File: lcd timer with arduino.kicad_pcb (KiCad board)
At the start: 2 copper layers, 121.1 x 76.4 mm, 33 parts, among them J1 Conn_01x05_Female, J2 Screw_Terminal_01x02, J3 Screw_Terminal_01x02, J4 Screw_Terminal_01x02, K1 SANYOU_SRD_Form_C, K2 SANYOU_SRD_Form_C, K3 SANYOU_SRD_Form_C, K4 SANYOU_SRD_Form_C, Q1 2N3904, Q2 2N3904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

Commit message: Version2
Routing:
- net on3: track 78.3 -> 75.6 mm

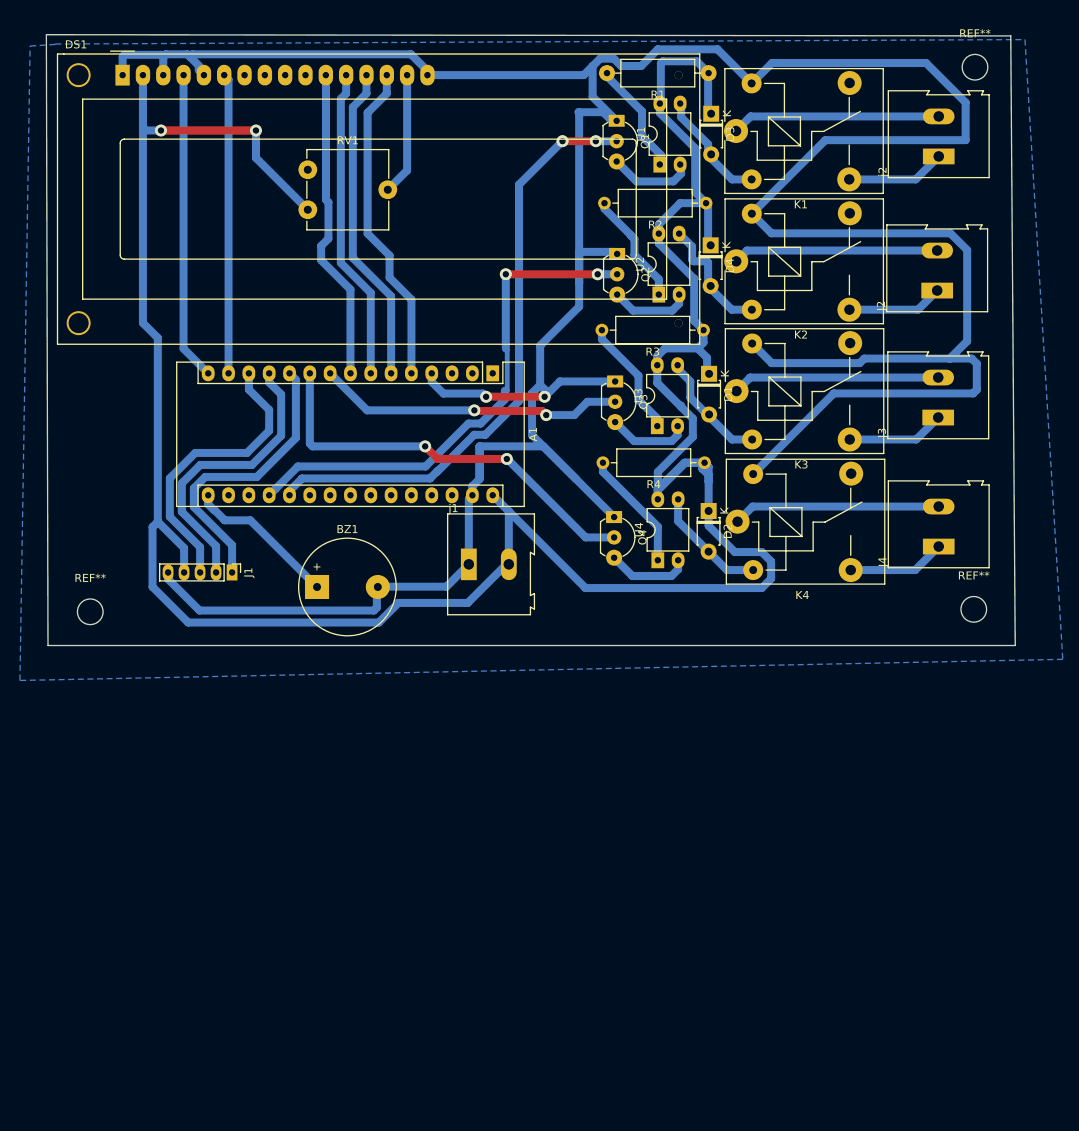
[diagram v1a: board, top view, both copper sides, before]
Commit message: thiker traces
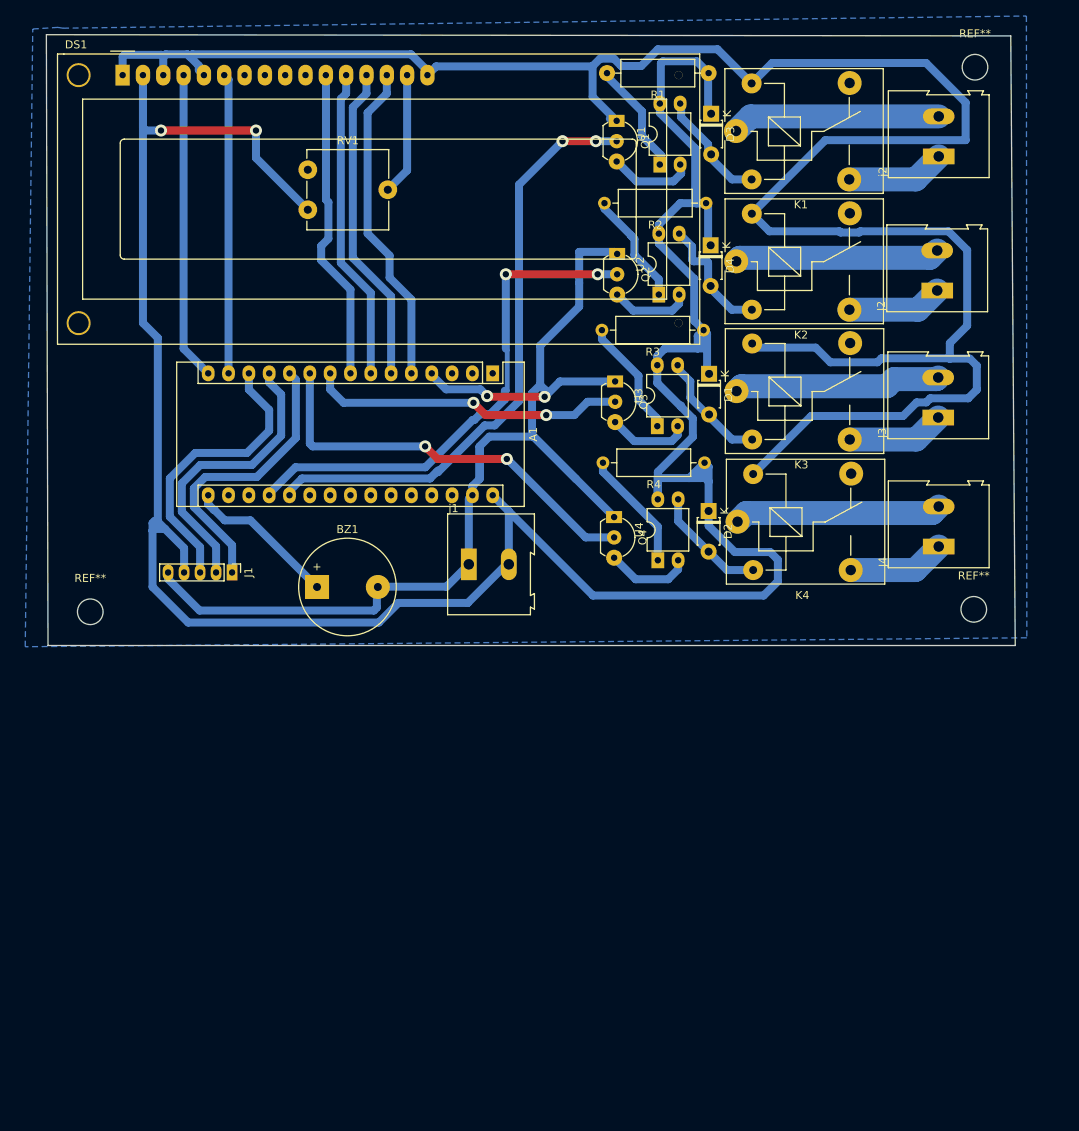
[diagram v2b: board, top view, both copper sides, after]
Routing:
- net -: track 448.1 -> 422.9 mm
- net +: track 335.0 -> 341.6 mm
- net on1: track 38.5 -> 39.6 mm

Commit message: removed acide traps
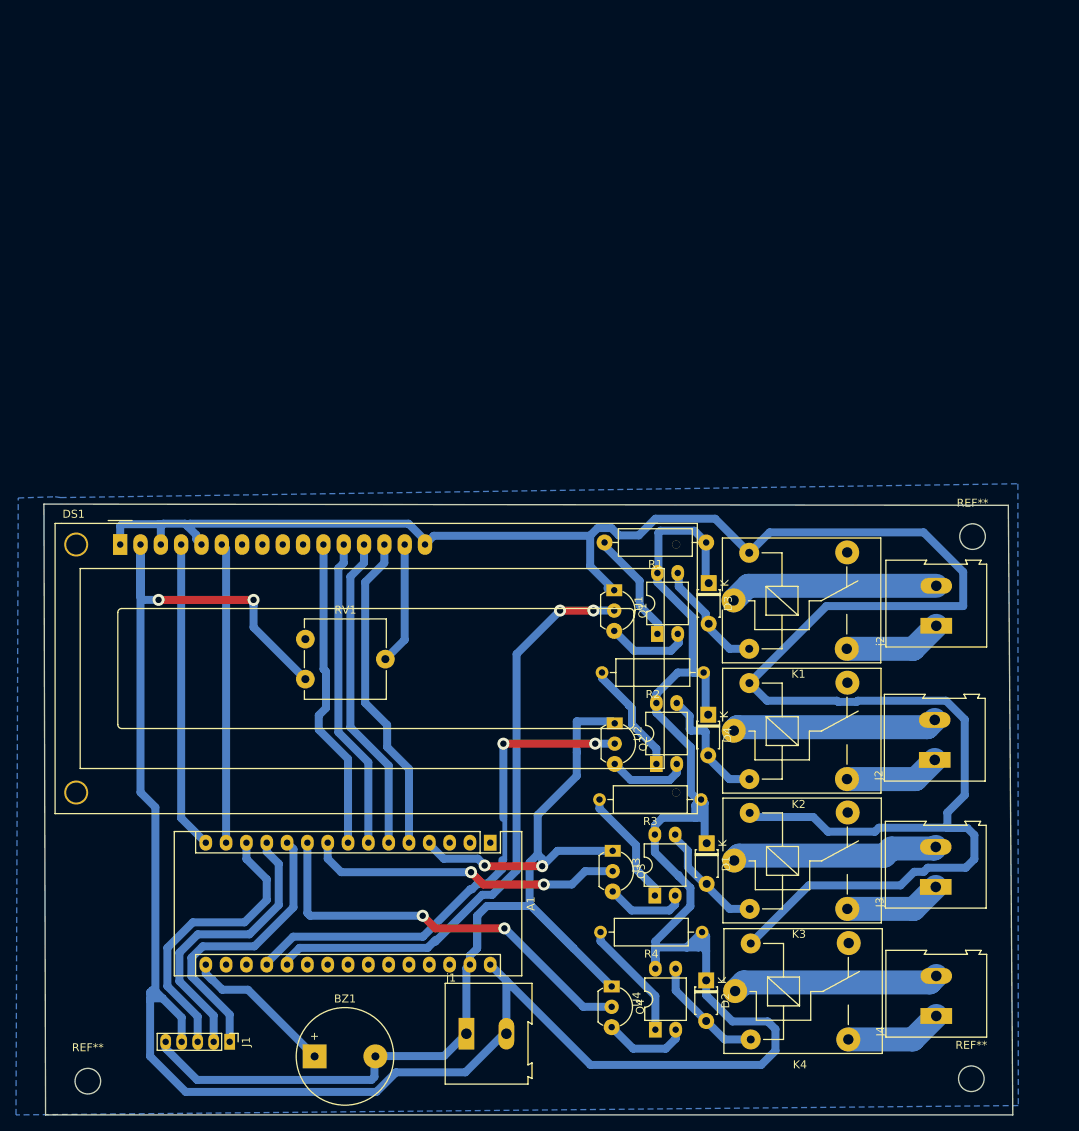
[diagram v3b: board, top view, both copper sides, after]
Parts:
- moved D1 58.7 mm to (150.0, 114.4)
- moved D2 58.7 mm to (149.9, 131.6)
- moved D3 58.7 mm to (150.3, 81.9)
- moved D4 58.7 mm to (150.2, 98.4)
- moved J1 58.7 mm to (90.4, 139.3)
- moved J2 58.7 mm to (178.5, 104.0)
- moved J3 58.7 mm to (178.6, 119.9)
- moved K2 58.7 mm to (153.4, 100.4)
- moved Q1 58.7 mm to (138.4, 82.8)
- moved Q4 58.7 mm to (138.1, 132.3)
- moved R4 58.7 mm to (149.4, 125.5)
- moved REF** 58.7 mm to (183.1, 143.9)
- moved REF** 58.7 mm to (72.6, 144.2)
- moved U4 58.7 mm to (143.6, 137.7)
- moved A1 58.7 mm to (122.9, 114.4)
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
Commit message: fixed the schematic
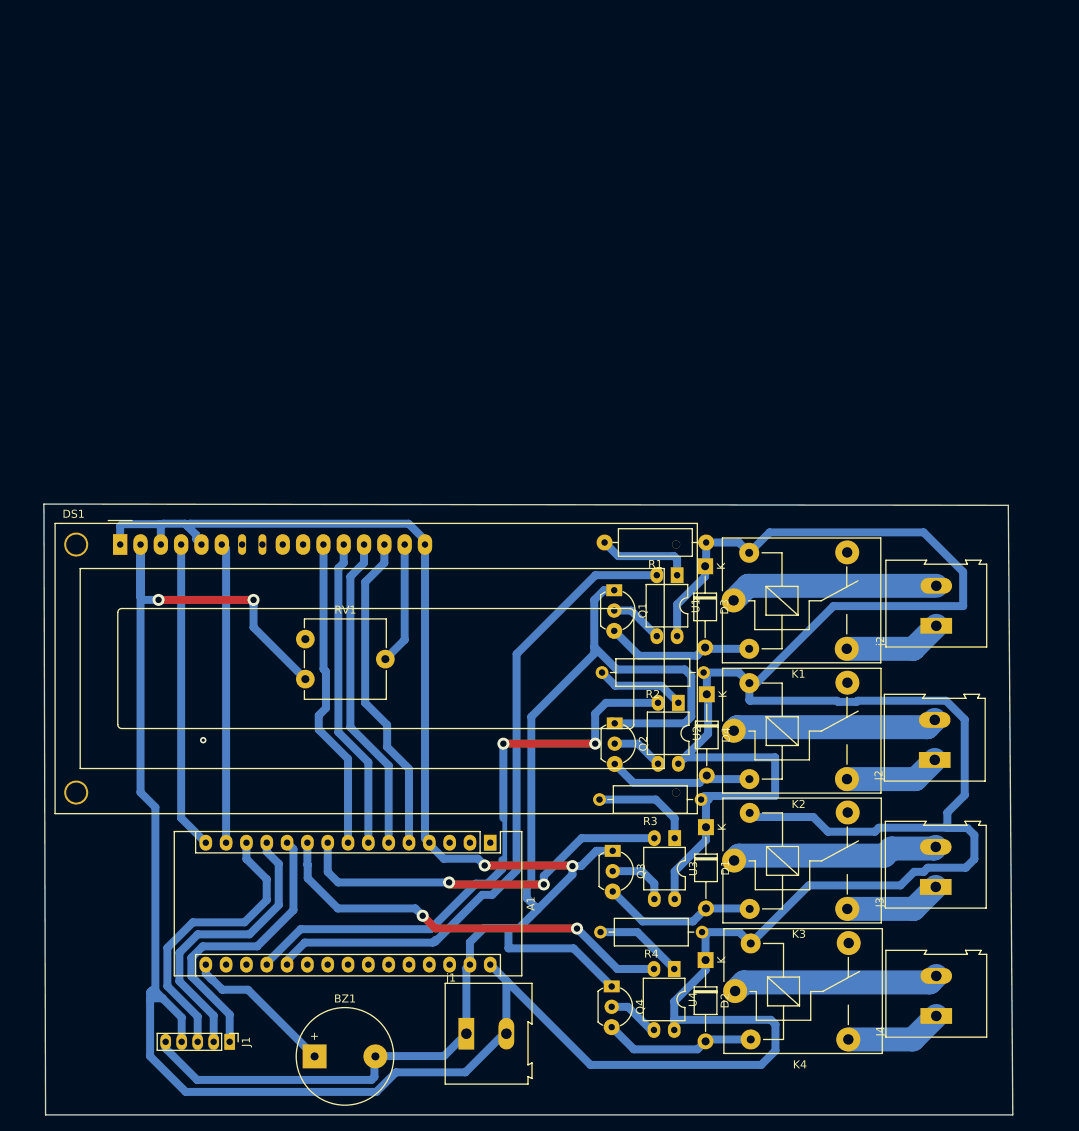
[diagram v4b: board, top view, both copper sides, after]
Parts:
- removed REF** (x3): MountingHole_3.2mm_M3, MountingHole:MountingHole_3.2mm_M3
- D1, D2, D3, D4: footprint Diode_THT:D_T-1_P5.08mm_Horizontal -> Diode_THT:D_T-1_P10.16mm_Horizontal
- moved U2 8.12 mm to (146.5, 96.9), turned to 270 degrees
- moved U4 7.94 mm to (145.9, 130.1), turned to 270 degrees
- moved U1 7.74 mm to (146.3, 80.9), turned to 270 degrees
- moved U3 7.59 mm to (146.0, 113.8), turned to 270 degrees
- moved D4 2.56 mm to (150.0, 95.8)
- moved D2 2.54 mm to (149.9, 129.0)
- moved D3 2.15 mm to (149.8, 79.8)
- moved D1 2.01 mm to (149.9, 112.4)
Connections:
- K1 pad 5: - -> +
- K2 pad 5: - -> +
- K3 pad 5: - -> +
- K4 pad 5: - -> +
- Q1 pad 2: on3 -> Net-(Q1-Pad2)
- Q1 pad 3: Net-(Q1-Pad3) -> Net-(D3-Pad2)
- Q2 pad 2: on4 -> Net-(Q2-Pad2)
- Q2 pad 3: Net-(Q2-Pad3) -> Net-(D4-Pad2)
- Q3 pad 2: on1 -> Net-(Q3-Pad2)
- Q3 pad 3: Net-(Q3-Pad3) -> Net-(D1-Pad2)
- Q4 pad 2: on2 -> Net-(Q4-Pad2)
- Q4 pad 3: Net-(Q4-Pad3) -> Net-(D2-Pad2)
- U1 pad 2: Net-(Q1-Pad3) -> on3
- U1 pad 3: Net-(D3-Pad2) -> Net-(Q1-Pad2)
- U2 pad 2: Net-(Q2-Pad3) -> on4
- U2 pad 3: Net-(D4-Pad2) -> Net-(Q2-Pad2)
- U3 pad 2: Net-(Q3-Pad3) -> on1
- U3 pad 3: Net-(D1-Pad2) -> Net-(Q3-Pad2)
- U4 pad 2: Net-(Q4-Pad3) -> on2
- U4 pad 3: Net-(D2-Pad2) -> Net-(Q4-Pad2)
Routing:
- net +: track 341.9 -> 497.8 mm
- net -: track 422.7 -> 274.9 mm
- net Net-(Q4-Pad3): track 10.8 -> 0.00 mm
- net Net-(Q1-Pad3): track 10.6 -> 0.00 mm
- net Net-(Q3-Pad3): track 10.2 -> 0.00 mm
- net Net-(Q2-Pad3): track 10.1 -> 0.00 mm
- net on4: track 64.5 -> 74.2 mm
- net on1: track 39.6 -> 48.2 mm
- net Net-(Q3-Pad2): track 0.00 -> 7.80 mm
- net on3: track 75.6 -> 82.8 mm, vias 2 -> 0
- net Net-(Q1-Pad2): track 0.00 -> 6.65 mm
- net Net-(Q4-Pad2): track 0.00 -> 6.48 mm
- net Net-(Q2-Pad2): track 0.00 -> 6.45 mm
- net Net-(D1-Pad2): track 14.6 -> 19.4 mm
- net Net-(D2-Pad2): track 14.6 -> 19.0 mm
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- removed copper zone on B.Cu, net -
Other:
- net class Default: clearance 0.4 -> 0.2
- rule trace_clearance: 0.4 -> 0.2

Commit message: fixed the schematic
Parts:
- added R5: 220, Resistor_THT:R_Axial_DIN0309_L9.0mm_D3.2mm_P12.70mm_Horizontal, F.Cu at (119.8, 88.6)
- moved RV1 11.2 mm to (109.7, 88.5), turned to 180 degrees
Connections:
- DS1 pad 15: Net-(DS1-Pad15) -> +
- DS1 pad 16: - -> Net-(DS1-Pad16)
- DS1 pad 3: - -> Net-(DS1-Pad3)
- RV1 pad 2: Net-(DS1-Pad15) -> Net-(DS1-Pad3)
- RV1 pad 3: Net-(RV1-Pad3) -> -
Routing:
- net Net-(DS1-Pad3): track 0.00 -> 27.7 mm, vias 0 -> 2
- net -: track 274.9 -> 301.5 mm
- net +: track 497.8 -> 518.5 mm
- net Net-(DS1-Pad15): track 15.3 -> 0.00 mm
- net Net-(DS1-Pad16): track 0.00 -> 14.2 mm
